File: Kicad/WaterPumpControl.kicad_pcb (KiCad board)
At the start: 2 copper layers, 91 x 79.8 mm, 53 parts, among them J1 Screw_Terminal_01x03, J10 Conn_02x03_Odd_Even, J2 Screw_Terminal_01x03, J3 Barrel_Jack_Switch, J4 Screw_Terminal_01x03, J5 Screw_Terminal_01x03, J6 Screw_Terminal_01x03, J7 Conn_01x06_Male, J8 Screw_Terminal_01x03, J9 Screw_Terminal_01x03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

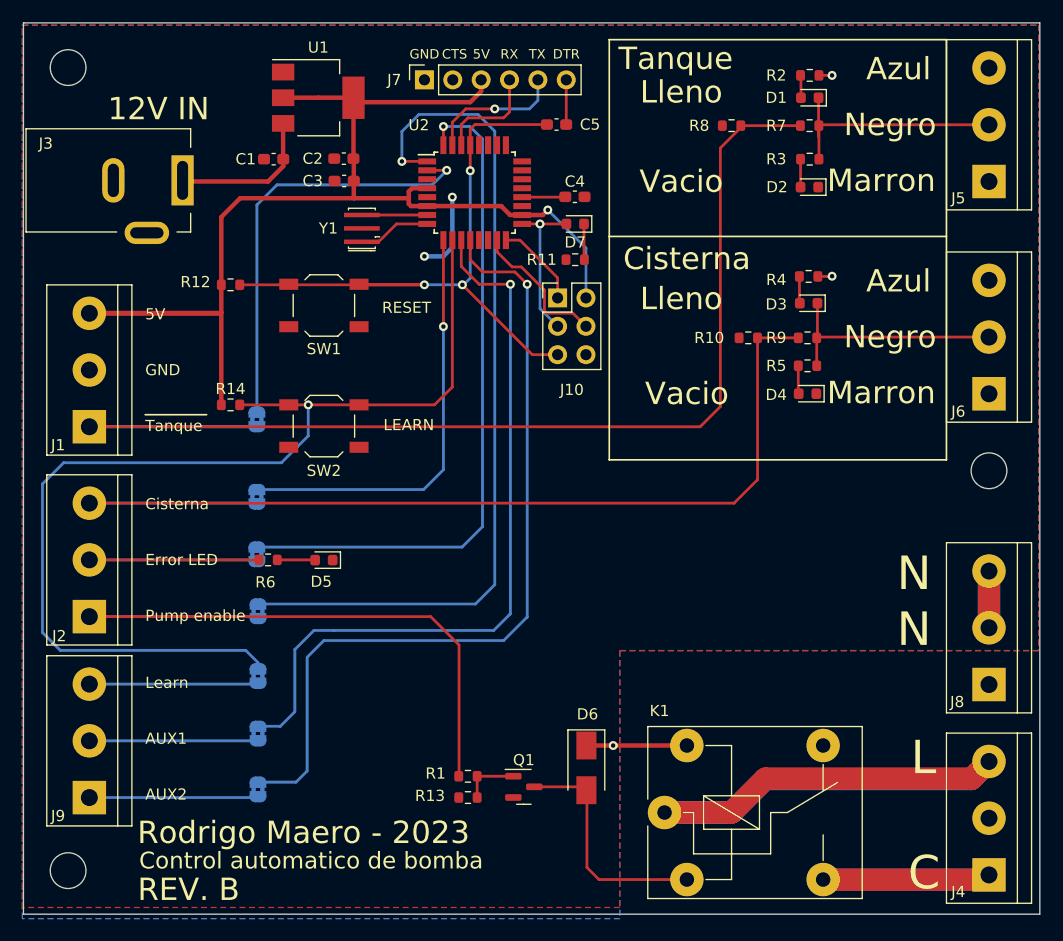
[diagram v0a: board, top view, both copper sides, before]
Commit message: Changed bottom plane from 12V to GND. Added silkscreen for ICSP.
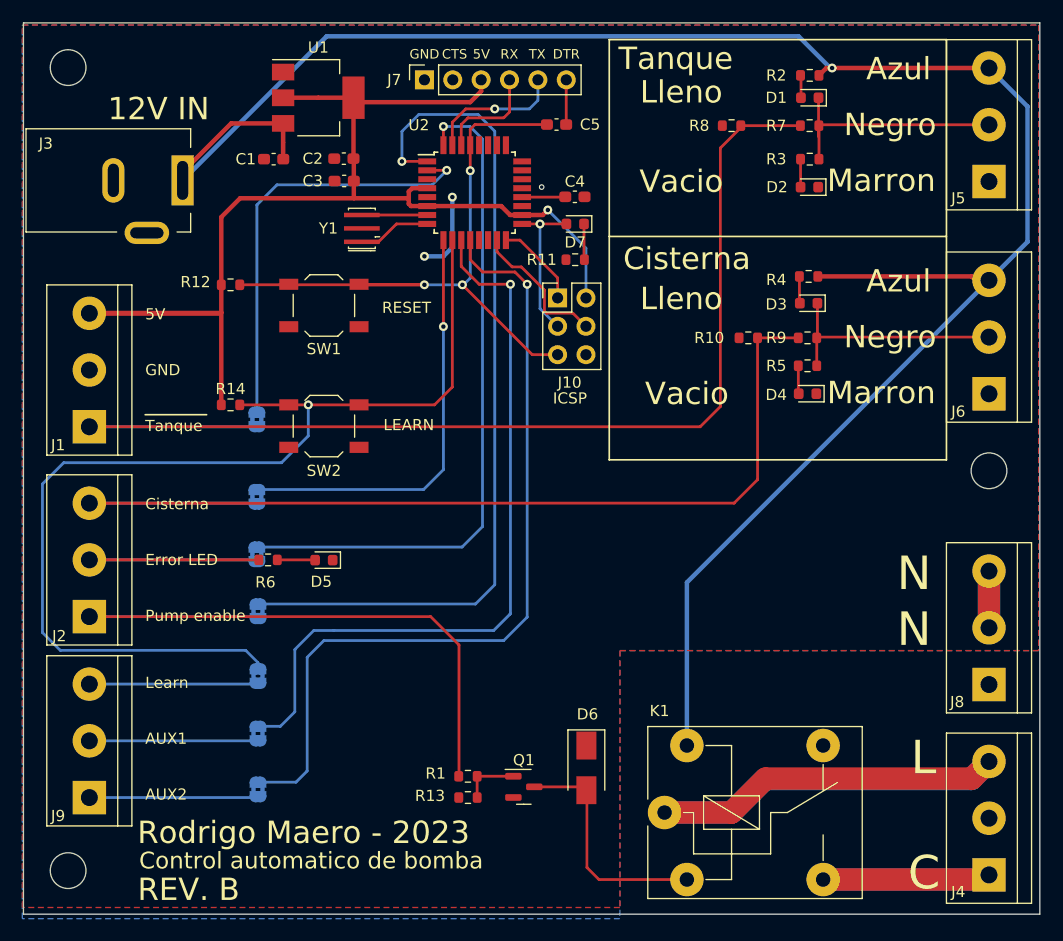
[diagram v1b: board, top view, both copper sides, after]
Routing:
- net +12V: track 30.8 -> 185.5 mm, vias 3 -> 1
- net GND: vias 2 -> 3
- added copper zone on B.Cu, net GND
- removed copper zone on B.Cu, net +12V
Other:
- board text added: "ICSP"
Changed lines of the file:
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@@
 		(tags "Through hole pin header THT 2x03 2.54mm double row")
 		(property "Reference" "J10"
-			(at 1.275 8.225 0)
+			(at 1.075 7.575 0)
 			(layer "F.SilkS")
 			(effects
@@
 		)
 	)
+	(gr_text "ICSP"
+		(at 67.5 54 0)
+		(layer "F.SilkS")
+		(effects
+			(font
+				(size 1 1)
+				(thickness 0.15)
+			)
+			(justify left bottom)
+		)
+	)
 	(gr_text "Marron"
 		(at 92.05 52.92 0)
@@
 	)
 	(segment
-		(start 79.5 84.5)
-		(end 72.9 84.5)
+		(start 105.35 42.85)
+		(end 105 42.5)
 		(width 0.4)
 		(layer "F.Cu")
@@
 	)
 	(segment
-		(start 92.5 24.5)
-		(end 91.512903 24.5)
-		(width 0.25)
+		(start 92.5 23.84)
+		(end 91.985 23.84)
+		(width 0.4)
 		(layer "F.Cu")
 		(net 1)
 	)
 	(segment
-		(start 72.9 84.5)
-		(end 70.5 84.5)
-		(width 0.4)
+		(start 35.05 34)
+		(end 34.45 33.4)
+		(width 0.25)
 		(layer "F.Cu")
 		(net 1)
 	)
 	(segment
-		(start 43.3625 32.6375)
-		(end 42 34)
+		(start 43.35 31.4875)
+		(end 43.35 30.5)
 		(width 0.4)
 		(layer "F.Cu")
@@
 	)
 	(segment
-		(start 35.05 34)
-		(end 34.45 33.4)
-		(width 0.25)
+		(start 38.7 28.8)
+		(end 43.35 28.8)
+		(width 0.4)
 		(layer "F.Cu")
 		(net 1)
 	)
 	(segment
-		(start 43.35 31.4875)
+		(start 43.35 30.5)
 		(end 43.35 28.8)
 		(width 0.4)
@@
 	)
 	(segment
-		(start 43.3625 32)
-		(end 43.3625 32.6375)
+		(start 92.5 23.84)
+		(end 106.55 23.84)
 		(width 0.4)
 		(layer "F.Cu")
@@
 	)
 	(segment
-		(start 42 34)
-		(end 35.05 34)
+		(start 34.35 33.9)
+		(end 34.35 33.15)
 		(width 0.4)
 		(layer "F.Cu")
@@
 	)
 	(segment
-		(start 92.5 42.480994)
-		(end 92.480994 42.5)
-		(width 0.25)
+		(start 34.35 33.15)
+		(end 38.7 28.8)
+		(width 0.4)
 		(layer "F.Cu")
 		(net 1)
 	)
 	(segment
-		(start 43.3625 31.5)
-		(end 43.35 31.4875)
-		(width 0.25)
+		(start 91.985 23.84)
+		(end 91.325 24.5)
+		(width 0.4)
 		(layer "F.Cu")
 		(net 1)
 	)
 	(segment
-		(start 92.480994 42.5)
+		(start 105 42.5)
 		(end 91.225 42.5)
+		(width 0.4)
+		(layer "F.Cu")
+		(net 1)
+	)
+	(segment
+		(start 106.55 42.85)
+		(end 105.35 42.85)
+		(width 0.4)
+		(layer "F.Cu")
+		(net 1)
+	)
+	(segment
+		(start 43.3625 31.5)
+		(end 43.35 31.4875)
 		(width 0.25)
 		(layer "F.Cu")
@@
 	)
 	(via
-		(at 92.5 24.5)
+		(at 92.5 23.84)
 		(size 0.8)
 		(drill 0.4)
 		(layers "F.Cu" "B.Cu")
-		(free yes)
 		(net 1)
 	)
-	(via
-		(at 92.5 42.480994)
-		(size 0.8)
-		(drill 0.4)
-		(layers "F.Cu" "B.Cu")
-		(free yes)
+	(segment
+		(start 106.55 42.85)
+		(end 110 39.4)
+		(width 0.4)
+		(layer "B.Cu")
 		(net 1)
 	)
-	(via
-		(at 72.9 84.5)
-		(size 0.8)
-		(drill 0.4)
-		(layers "F.Cu" "B.Cu")
+	(segment
+		(start 106.55 42.85)
+		(end 79.5 69.9)
+		(width 0.4)
+		(layer "B.Cu")
 		(net 1)
 	)
 	(segment
-		(start 79.5 84.5)
-		(end 73 84.5)
-		(width 0.25)
+		(start 79.5 69.9)
+		(end 79.5 84.5)
+		(width 0.4)
+		(layer "B.Cu")
+		(net 1)
+	)
+	(segment
+		(start 47.25 21)
+		(end 89.5 21)
+		(width 0.4)
+		(layer "B.Cu")
+		(net 1)
+	)
+	(segment
+		(start 89.5 21)
+		(end 92.34 23.84)
+		(width 0.4)
+		(layer "B.Cu")
+		(net 1)
+	)
+	(segment
+		(start 110 39.4)
+		(end 110 27.29)
+		(width 0.4)
+		(layer "B.Cu")
+		(net 1)
+	)
+	(segment
+		(start 34.35 33.9)
+		(end 47.25 21)
+		(width 0.4)
+		(layer "B.Cu")
+		(net 1)
+	)
+	(segment
+		(start 110 27.29)
+		(end 106.55 23.84)
+		(width 0.4)
+		(layer "B.Cu")
+		(net 1)
+	)
+	(segment
+		(start 92.34 23.84)
+		(end 92.5 23.84)
+		(width 0.4)
 		(layer "B.Cu")
 		(net 1)
@@
 	)
 	(via
+		(at 66.5 34.5)
+		(size 0.5)
+		(drill 0.3)
+		(layers "F.Cu" "B.Cu")
+		(free yes)
+		(net 42)
+	)
+	(via
 		(at 58.5 35.4)
 		(size 0.8)
@@
 	)
 	(zone
-		(net 1)
-		(net_name "+12V")
+		(net 42)
+		(net_name "GND")
 		(layer "B.Cu")
 		(hatch edge 0.508)
